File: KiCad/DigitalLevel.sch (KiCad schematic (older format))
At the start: 71 parts, among them SW1 Power-Up Button, SW2 Horizontal, SW3 Vertical, SW4 Reset Button, U2 MPU-6050, U3 XC6206P332MR

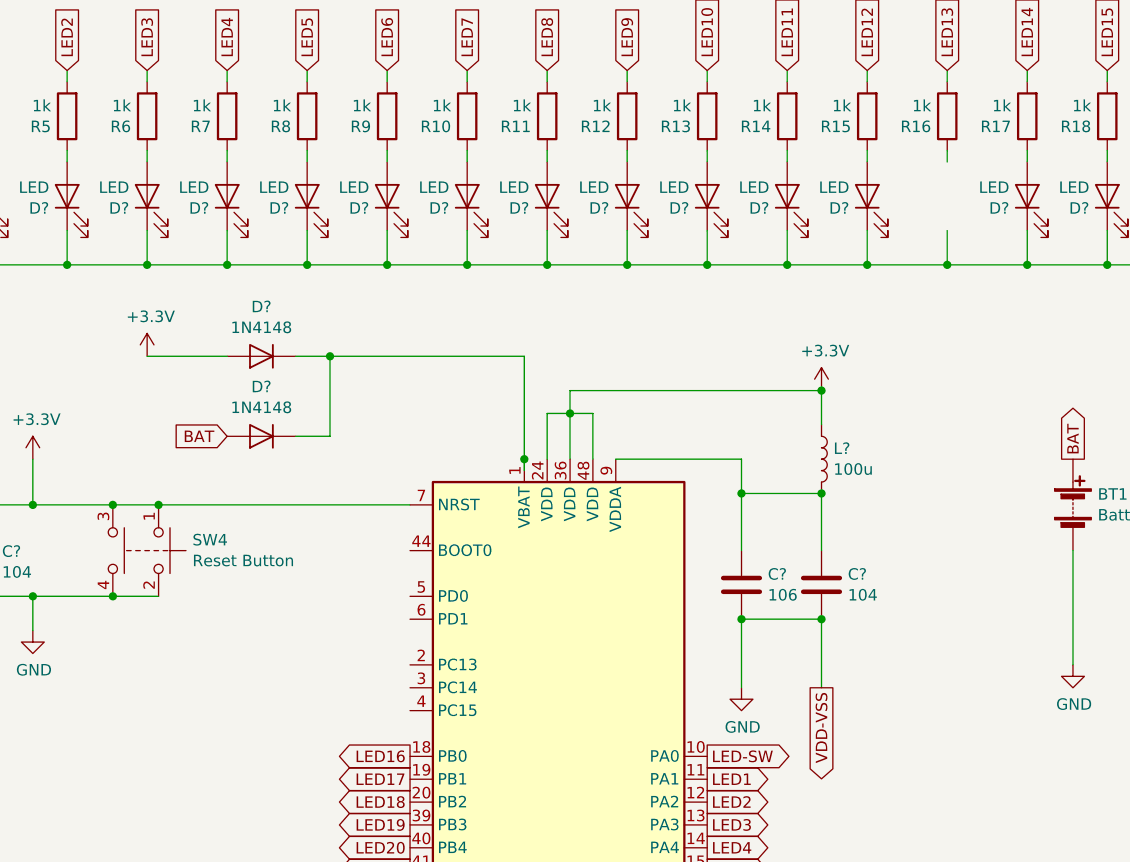
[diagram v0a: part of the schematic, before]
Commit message: Fixed schematics
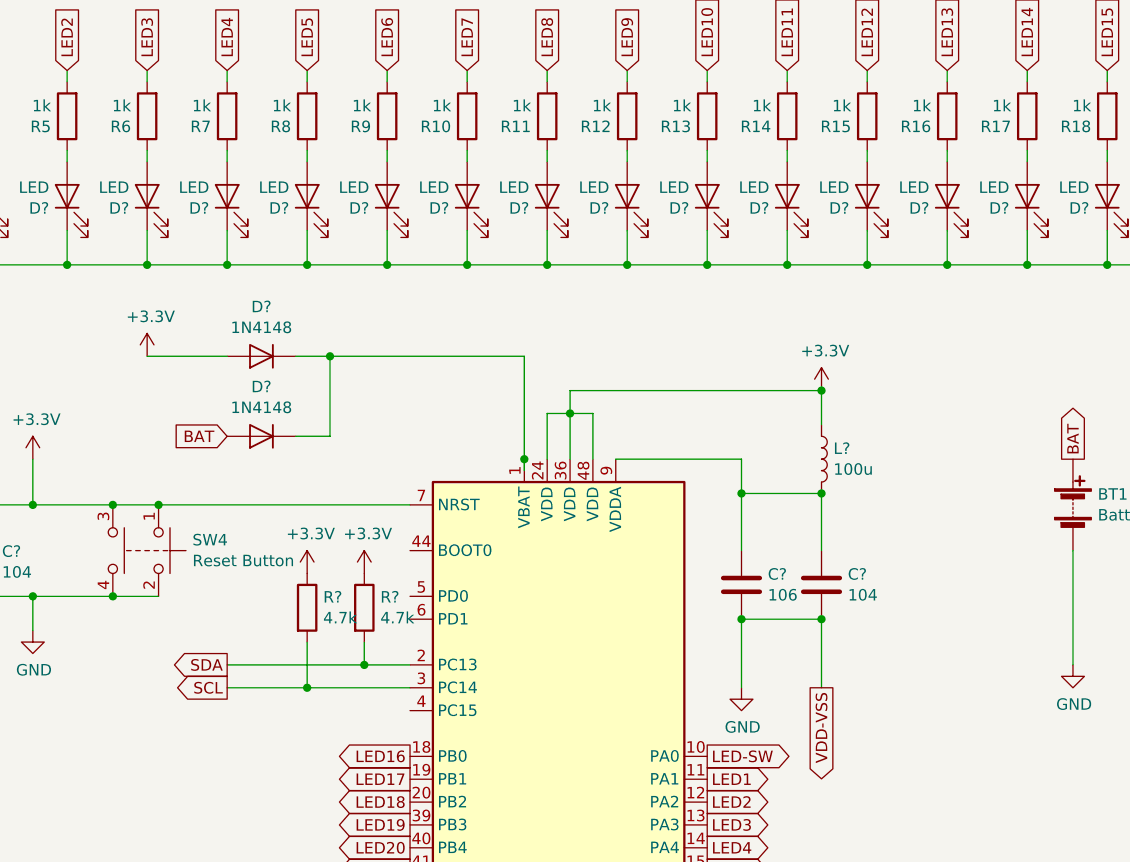
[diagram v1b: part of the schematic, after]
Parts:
- added D?: LED, symbol Device:LED
- added R? (x2): 4.7k, symbol Device:R
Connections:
- net +3V3: now also R?.1, R?.1
- net GND: now also D?.1 (K)
- net SCL: now also U?.3 (PC14), R?.2
- net SDA: now also U?.2 (PC13), R?.2
- net at R16.1: now also D?.2 (A)
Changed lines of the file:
@@
 	2250 1400 2250 1350
-Wire Wire Line
-	6450 1400 6450 1350
 Wire Wire Line
 	6800 1400 6800 1350
@@
 Wire Wire Line
 	6800 1700 6800 1850
-Wire Wire Line
-	6450 1700 6450 1850
 Wire Wire Line
 	6100 1700 6100 1850
@@
 Text GLabel 4100 5100 0    50   Input ~ 0
 BTN3
+Wire Wire Line
+	6450 1700 6450 1850
+Wire Wire Line
+	6450 1400 6450 1350
+$Comp
+L Device:LED D?
+U 1 1 5ED0B1A6
+P 6450 1550
+F 0 "D?" V 6397 1628 50  0000 L CNN
+F 1 "LED" V 6488 1628 50  0000 L CNN
+F 2 "" H 6450 1550 50  0001 C CNN
+F 3 "~" H 6450 1550 50  0001 C CNN
+	1    6450 1550
+	0    -1   -1   0
+$EndComp
+Wire Wire Line
+	3900 3500 3900 3600
+Wire Wire Line
+	3650 3700 3650 3500
+Connection ~ 3650 3700
+Wire Wire Line
+	3650 3700 3300 3700
+$Comp
+L Device:R R?
+U 1 1 5ED6A549
+P 3900 3350
+F 0 "R?" H 3970 3396 50  0000 L CNN
+F 1 "4.7k" H 3970 3305 50  0000 L CNN
+F 2 "" V 3830 3350 50  0001 C CNN
+F 3 "~" H 3900 3350 50  0001 C CNN
+	1    3900 3350
+	1    0    0    -1
+$EndComp
+$Comp
+L Device:R R?
+U 1 1 5ED6B787
+P 3650 3350
+F 0 "R?" H 3720 3396 50  0000 L CNN
+F 1 "4.7k" H 3720 3305 50  0000 L CNN
+F 2 "" V 3580 3350 50  0001 C CNN
+F 3 "~" H 3650 3350 50  0001 C CNN
+	1    3650 3350
+	1    0    0    -1
+$EndComp
+$Comp
+L power:+3.3V #PWR?
+U 1 1 5ED6C7CF
+P 3650 3200
+F 0 "#PWR?" H 3650 3050 50  0001 C CNN
+F 1 "+3.3V" H 3665 3373 50  0000 C CNN
+F 2 "" H 3650 3200 50  0001 C CNN
+F 3 "" H 3650 3200 50  0001 C CNN
+	1    3650 3200
+	1    0    0    -1
+$EndComp
+$Comp
+L power:+3.3V #PWR?
+U 1 1 5ED6DF7F
+P 3900 3200
+F 0 "#PWR?" H 3900 3050 50  0001 C CNN
+F 1 "+3.3V" H 3915 3373 50  0000 C CNN
+F 2 "" H 3900 3200 50  0001 C CNN
+F 3 "" H 3900 3200 50  0001 C CNN
+	1    3900 3200
+	1    0    0    -1
+$EndComp
+Wire Wire Line
+	3300 3600 3900 3600
+Connection ~ 3900 3600
+Wire Wire Line
+	3900 3600 4100 3600
+Wire Wire Line
+	3650 3700 4100 3700
+Text GLabel 3300 3600 0    50   Output ~ 0
+SDA
+Text GLabel 3300 3700 0    50   Output ~ 0
+SCL
 $EndSCHEMATC
